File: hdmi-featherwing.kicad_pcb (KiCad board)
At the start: 2 copper layers, 22.9 x 50.8 mm, 10 parts, among them J1 HDMI_A

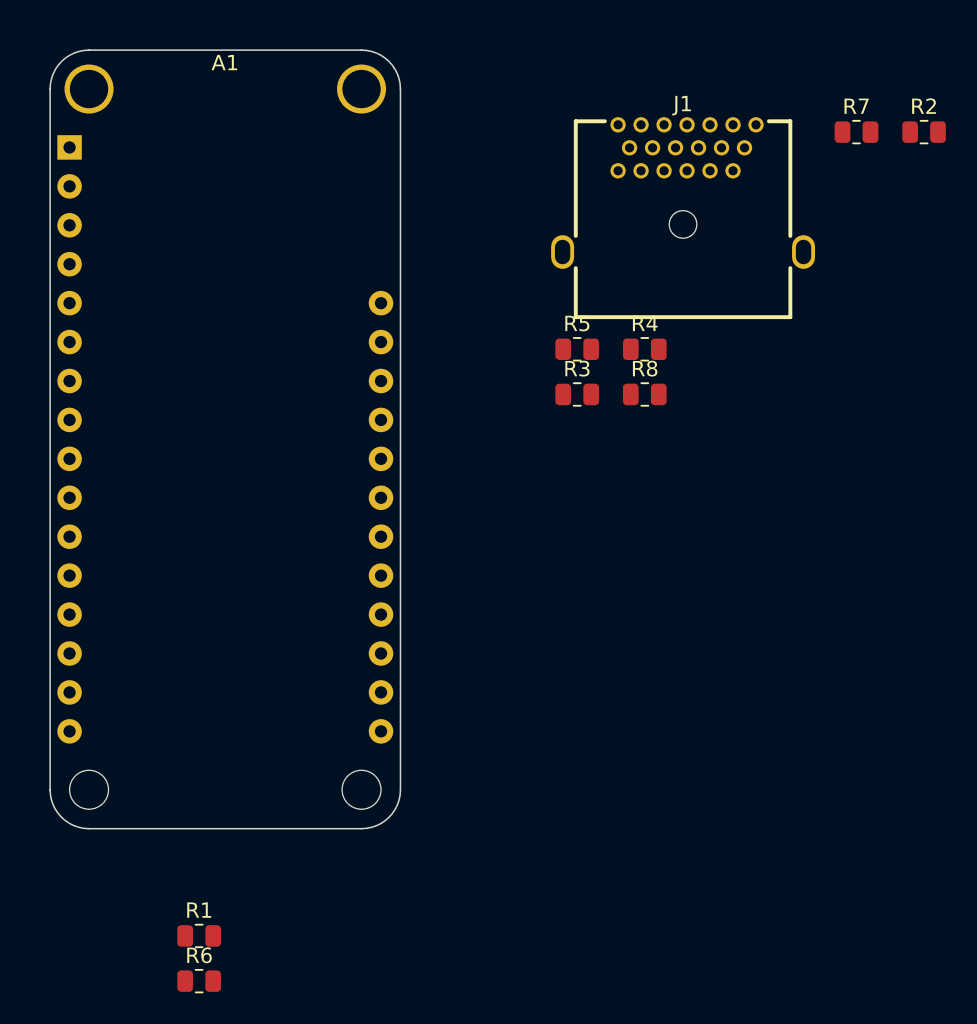
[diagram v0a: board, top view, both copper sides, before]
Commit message: Add CK resistors
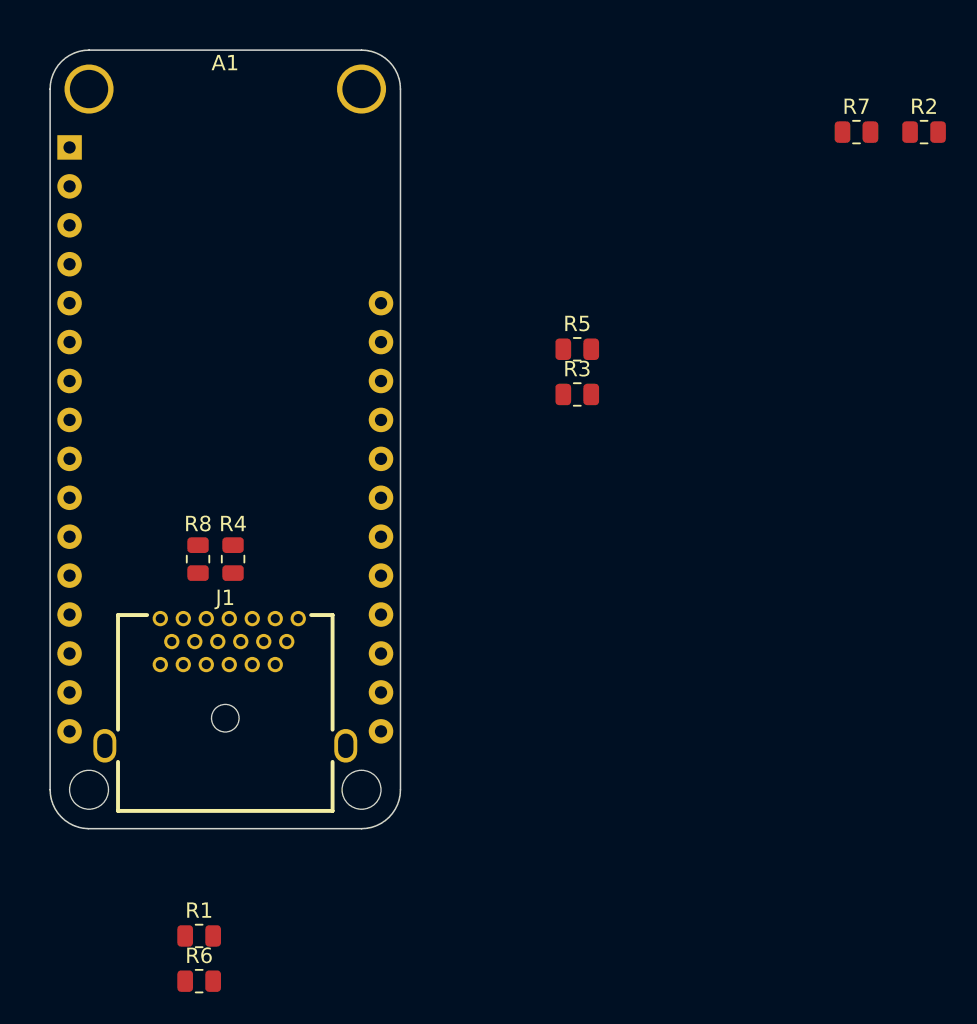
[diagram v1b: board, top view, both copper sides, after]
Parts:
- moved J1 43.9 mm to (119.4, 120.0)
- moved R8 31.1 mm to (117.6, 112.0), turned to -90 degrees
- moved R4 30.2 mm to (119.9, 112.0), turned to -90 degrees
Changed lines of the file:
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@@
   )
   (footprint "Resistor_SMD:R_0805_2012Metric" (layer "F.Cu")
-    (at 146.754 98.259)
-    (descr "Resistor SMD 0805 (2012 Metric), square (rectangular) end terminal, IPC_7351 nominal, (Body size source: IPC-SM-782 page 72, https://www.pcb-3d.com/wordpress/wp-content/uploads/ipc-sm-782a_amendment_1_and_2.pdf), generated with kicad-footprint-generator")
-    (tags "resistor")
-    (property "Sheetfile" "hdmi-featherwing.kicad_sch")
-    (property "Sheetname" "")
-    (attr smd)
-    (fp_text reference "R4" (at 0 -1.65) (layer "F.SilkS")
-      (effects (font (size 1 1) (thickness 0.15)))
-    )
-    (fp_text value "270" (at 0 1.65) (layer "F.Fab")
-      (effects (font (size 1 1) (thickness 0.15)))
-    )
-    (fp_text user "${REFERENCE}" (at 0 0) (layer "F.Fab")
-      (effects (font (size 0.5 0.5) (thickness 0.08)))
-    )
-    (fp_line (start -0.227064 -0.735) (end 0.227064 -0.735) (layer "F.SilkS") (width 0.12))
-    (fp_line (start -0.227064 0.735) (end 0.227064 0.735) (layer "F.SilkS") (width 0.12))
-    (fp_line (start 1.68 -0.95) (end 1.68 0.95) (layer "F.CrtYd") (width 0.05))
-    (fp_line (start 1.68 0.95) (end -1.68 0.95) (layer "F.CrtYd") (width 0.05))
-    (fp_line (start -1.68 -0.95) (end 1.68 -0.95) (layer "F.CrtYd") (width 0.05))
-    (fp_line (start -1.68 0.95) (end -1.68 -0.95) (layer "F.CrtYd") (width 0.05))
-    (fp_line (start 1 -0.625) (end 1 0.625) (layer "F.Fab") (width 0.1))
-    (fp_line (start 1 0.625) (end -1 0.625) (layer "F.Fab") (width 0.1))
-    (fp_line (start -1 0.625) (end -1 -0.625) (layer "F.Fab") (width 0.1))
-    (fp_line (start -1 -0.625) (end 1 -0.625) (layer "F.Fab") (width 0.1))
-    (pad "1" smd roundrect (at -0.9125 0) (locked) (size 1.025 1.4) (layers "F.Cu" "F.Paste" "F.Mask") (roundrect_rratio 0.243902)
+    (at 119.888 111.951 -90)
+    (descr "Resistor SMD 0805 (2012 Metric), square (rectangular) end terminal, IPC_7351 nominal, (Body size source: IPC-SM-782 page 72, https://www.pcb-3d.com/wordpress/wp-content/uploads/ipc-sm-782a_amendment_1_and_2.pdf), generated with kicad-footprint-generator")
+    (tags "resistor")
+    (property "Sheetfile" "hdmi-featherwing.kicad_sch")
+    (property "Sheetname" "")
+    (attr smd)
+    (fp_text reference "R4" (at -2.286 0 180) (layer "F.SilkS")
+      (effects (font (size 1 1) (thickness 0.15)))
+    )
+    (fp_text value "270" (at 0 1.650009 90) (layer "F.Fab") hide
+      (effects (font (size 1 1) (thickness 0.15)))
+    )
+    (fp_text user "${REFERENCE}" (at 0 0 90) (layer "F.Fab")
+      (effects (font (size 0.5 0.5) (thickness 0.08)))
+    )
+    (fp_line (start -0.227064 -0.735) (end 0.227064 -0.735) (layer "F.SilkS") (width 0.12))
+    (fp_line (start -0.227064 0.735) (end 0.227064 0.735) (layer "F.SilkS") (width 0.12))
+    (fp_line (start 1.68 -0.95) (end 1.68 0.95) (layer "F.CrtYd") (width 0.05))
+    (fp_line (start 1.68 0.95) (end -1.68 0.95) (layer "F.CrtYd") (width 0.05))
+    (fp_line (start -1.68 -0.95) (end 1.68 -0.95) (layer "F.CrtYd") (width 0.05))
+    (fp_line (start -1.68 0.95) (end -1.68 -0.95) (layer "F.CrtYd") (width 0.05))
+    (fp_line (start 1 -0.625) (end 1 0.625) (layer "F.Fab") (width 0.1))
+    (fp_line (start 1 0.625) (end -1 0.625) (layer "F.Fab") (width 0.1))
+    (fp_line (start -1 0.625) (end -1 -0.625) (layer "F.Fab") (width 0.1))
+    (fp_line (start -1 -0.625) (end 1 -0.625) (layer "F.Fab") (width 0.1))
+    (pad "1" smd roundrect (at -0.9125 0 270) (locked) (size 1.025 1.4) (layers "F.Cu" "F.Paste" "F.Mask") (roundrect_rratio 0.243902)
       (net 21 "/WING_CK+") (pintype "passive"))
-    (pad "2" smd roundrect (at 0.9125 0) (locked) (size 1.025 1.4) (layers "F.Cu" "F.Paste" "F.Mask") (roundrect_rratio 0.243902)
+    (pad "2" smd roundrect (at 0.9125 0 270) (locked) (size 1.025 1.4) (layers "F.Cu" "F.Paste" "F.Mask") (roundrect_rratio 0.243902)
       (net 35 "Net-(J1-Pad10)") (pintype "passive"))
     (model "${KICAD6_3DMODEL_DIR}/Resistor_SMD.3dshapes/R_0805_2012Metric.wrl"
@@
   )
   (footprint "HDMI:HDMI-TH_HYC12-HDMIA19-61" (layer "F.Cu")
-    (at 149.249 87.764)
+    (at 119.38 119.9815)
     (property "Sheetfile" "hdmi-featherwing.kicad_sch")
     (property "Sheetname" "")
@@
   )
   (footprint "Resistor_SMD:R_0805_2012Metric" (layer "F.Cu")
-    (at 146.754 101.209)
-    (descr "Resistor SMD 0805 (2012 Metric), square (rectangular) end terminal, IPC_7351 nominal, (Body size source: IPC-SM-782 page 72, https://www.pcb-3d.com/wordpress/wp-content/uploads/ipc-sm-782a_amendment_1_and_2.pdf), generated with kicad-footprint-generator")
-    (tags "resistor")
-    (property "Sheetfile" "hdmi-featherwing.kicad_sch")
-    (property "Sheetname" "")
-    (attr smd)
-    (fp_text reference "R8" (at 0 -1.65) (layer "F.SilkS")
-      (effects (font (size 1 1) (thickness 0.15)))
-    )
-    (fp_text value "270" (at 0 1.65) (layer "F.Fab")
-      (effects (font (size 1 1) (thickness 0.15)))
-    )
-    (fp_text user "${REFERENCE}" (at 0 0) (layer "F.Fab")
-      (effects (font (size 0.5 0.5) (thickness 0.08)))
-    )
-    (fp_line (start -0.227064 0.735) (end 0.227064 0.735) (layer "F.SilkS") (width 0.12))
-    (fp_line (start -0.227064 -0.735) (end 0.227064 -0.735) (layer "F.SilkS") (width 0.12))
-    (fp_line (start 1.68 0.95) (end -1.68 0.95) (layer "F.CrtYd") (width 0.05))
-    (fp_line (start -1.68 -0.95) (end 1.68 -0.95) (layer "F.CrtYd") (width 0.05))
-    (fp_line (start 1.68 -0.95) (end 1.68 0.95) (layer "F.CrtYd") (width 0.05))
-    (fp_line (start -1.68 0.95) (end -1.68 -0.95) (layer "F.CrtYd") (width 0.05))
-    (fp_line (start 1 -0.625) (end 1 0.625) (layer "F.Fab") (width 0.1))
-    (fp_line (start -1 -0.625) (end 1 -0.625) (layer "F.Fab") (width 0.1))
-    (fp_line (start 1 0.625) (end -1 0.625) (layer "F.Fab") (width 0.1))
-    (fp_line (start -1 0.625) (end -1 -0.625) (layer "F.Fab") (width 0.1))
-    (pad "1" smd roundrect (at -0.9125 0) (locked) (size 1.025 1.4) (layers "F.Cu" "F.Paste" "F.Mask") (roundrect_rratio 0.243902)
+    (at 117.602 111.951 -90)
+    (descr "Resistor SMD 0805 (2012 Metric), square (rectangular) end terminal, IPC_7351 nominal, (Body size source: IPC-SM-782 page 72, https://www.pcb-3d.com/wordpress/wp-content/uploads/ipc-sm-782a_amendment_1_and_2.pdf), generated with kicad-footprint-generator")
+    (tags "resistor")
+    (property "Sheetfile" "hdmi-featherwing.kicad_sch")
+    (property "Sheetname" "")
+    (attr smd)
+    (fp_text reference "R8" (at -2.286 0 180) (layer "F.SilkS")
+      (effects (font (size 1 1) (thickness 0.15)))
+    )
+    (fp_text value "270" (at 0.000005 1.650009 90) (layer "F.Fab") hide
+      (effects (font (size 1 1) (thickness 0.15)))
+    )
+    (fp_text user "${REFERENCE}" (at 0 0 90) (layer "F.Fab")
+      (effects (font (size 0.5 0.5) (thickness 0.08)))
+    )
+    (fp_line (start -0.227064 0.735) (end 0.227064 0.735) (layer "F.SilkS") (width 0.12))
+    (fp_line (start -0.227064 -0.735) (end 0.227064 -0.735) (layer "F.SilkS") (width 0.12))
+    (fp_line (start 1.68 0.95) (end -1.68 0.95) (layer "F.CrtYd") (width 0.05))
+    (fp_line (start -1.68 -0.95) (end 1.68 -0.95) (layer "F.CrtYd") (width 0.05))
+    (fp_line (start 1.68 -0.95) (end 1.68 0.95) (layer "F.CrtYd") (width 0.05))
+    (fp_line (start -1.68 0.95) (end -1.68 -0.95) (layer "F.CrtYd") (width 0.05))
+    (fp_line (start 1 -0.625) (end 1 0.625) (layer "F.Fab") (width 0.1))
+    (fp_line (start -1 -0.625) (end 1 -0.625) (layer "F.Fab") (width 0.1))
+    (fp_line (start 1 0.625) (end -1 0.625) (layer "F.Fab") (width 0.1))
+    (fp_line (start -1 0.625) (end -1 -0.625) (layer "F.Fab") (width 0.1))
+    (pad "1" smd roundrect (at -0.9125 0 270) (locked) (size 1.025 1.4) (layers "F.Cu" "F.Paste" "F.Mask") (roundrect_rratio 0.243902)
       (net 22 "/WING_CK-") (pintype "passive"))
-    (pad "2" smd roundrect (at 0.9125 0) (locked) (size 1.025 1.4) (layers "F.Cu" "F.Paste" "F.Mask") (roundrect_rratio 0.243902)
+    (pad "2" smd roundrect (at 0.9125 0 270) (locked) (size 1.025 1.4) (layers "F.Cu" "F.Paste" "F.Mask") (roundrect_rratio 0.243902)
       (net 34 "Net-(J1-Pad12)") (pintype "passive"))
     (model "${KICAD6_3DMODEL_DIR}/Resistor_SMD.3dshapes/R_0805_2012Metric.wrl"

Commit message: Label differential pair nets
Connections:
- net Net-(J1-Pad1) renamed /D2+
- net Net-(J1-Pad10) renamed /CK+
- net Net-(J1-Pad12) renamed /CK-
- net Net-(J1-Pad3) renamed /D2-
- net Net-(J1-Pad4) renamed /D1+
- net Net-(J1-Pad6) renamed /D1-
- net Net-(J1-Pad7) renamed /D0+
- net Net-(J1-Pad9) renamed /D0-

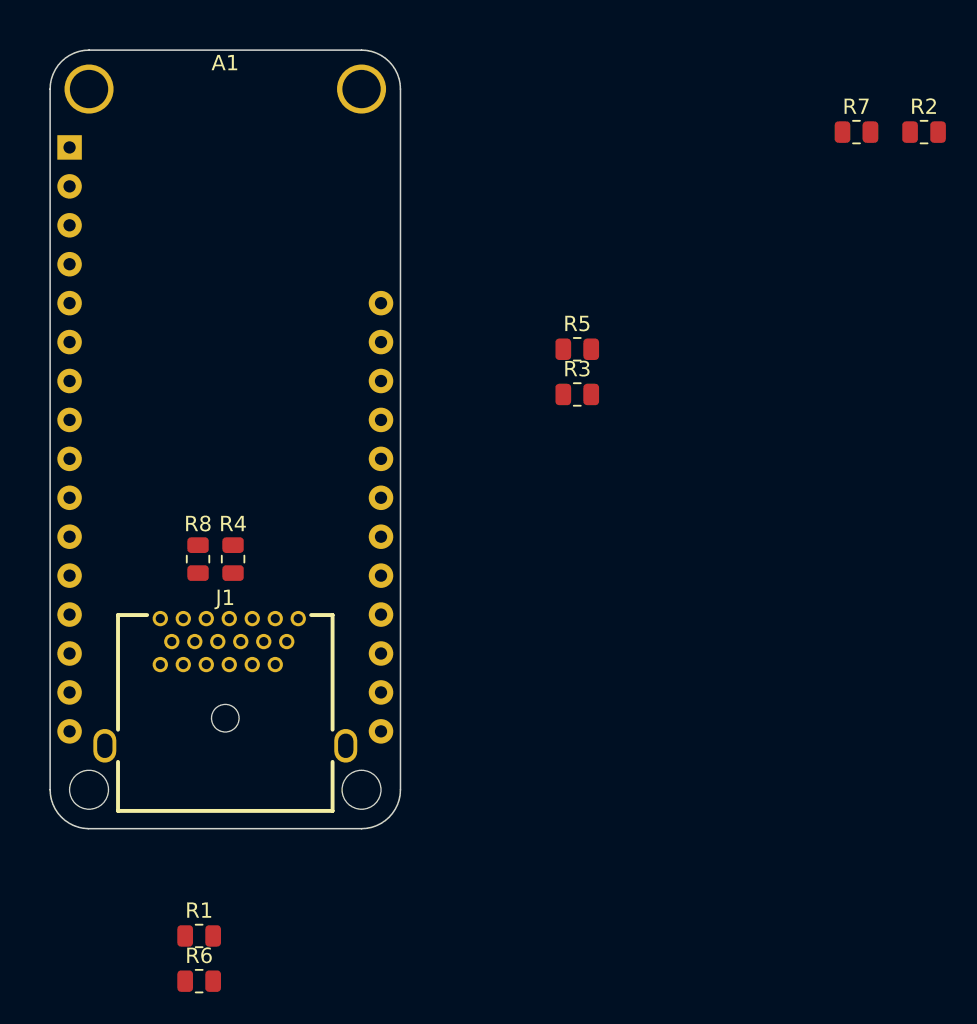
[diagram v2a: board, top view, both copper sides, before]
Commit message: Route resistors
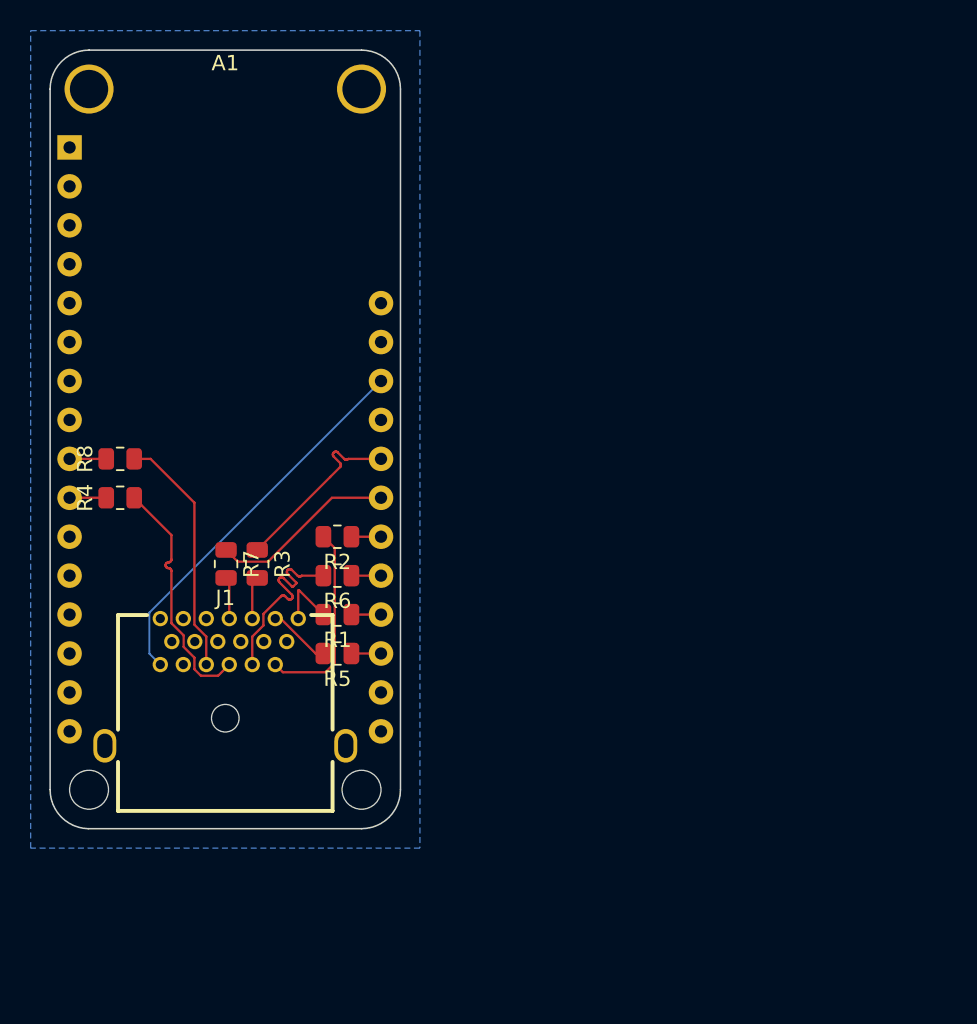
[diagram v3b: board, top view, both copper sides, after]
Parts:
- moved R7 49.9 mm to (119.4, 112.3), turned to -90 degrees
- moved R2 46.5 mm to (126.7, 110.5), turned to 180 degrees
- moved R6 28.0 mm to (126.7, 113.0), turned to 180 degrees
- moved R5 25.3 mm to (126.7, 118.1), turned to 180 degrees
- moved R3 23.6 mm to (121.5, 112.3), turned to -90 degrees
- moved R1 22.8 mm to (126.7, 115.6), turned to 180 degrees
- moved R4 8.38 mm to (112.5, 108.0), turned to 0 degrees
- moved R8 8.28 mm to (112.5, 105.4), turned to 0 degrees
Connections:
- A1 pad 10: /WING_CK- -> /WING_CK+
- A1 pad 19: /WING_D2+ -> /WING_D2-
- A1 pad 20: /WING_D2- -> /WING_D2+
- A1 pad 21: /WING_D1+ -> /WING_D1-
- A1 pad 22: /WING_D1- -> /WING_D1+
- A1 pad 23: /WING_D0+ -> /WING_D0-
- A1 pad 24: /WING_D0- -> /WING_D0+
- A1 pad 9: /WING_CK+ -> /WING_CK-
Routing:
- net +5V: track 0.00 -> 25.1 mm
- net /CK+: track 0.00 -> 16.0 mm
- net /CK-: track 0.00 -> 16.0 mm
- net /D1-: track 0.00 -> 12.9 mm
- net /D1+: track 0.00 -> 12.9 mm
- net /WING_D0+: track 0.00 -> 12.1 mm
- net /WING_D0-: track 0.00 -> 12.1 mm
- net /D2+: track 0.00 -> 4.13 mm
- net /D2-: track 0.00 -> 4.09 mm
- net /D0+: track 0.00 -> 2.78 mm
- net /D0-: track 0.00 -> 2.74 mm
- net /WING_CK-: track 0.00 -> 2.39 mm
- net /WING_CK+: track 0.00 -> 2.39 mm
- net /WING_D1+: track 0.00 -> 1.93 mm
- net /WING_D2-: track 0.00 -> 1.93 mm
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- added copper zone on B.Cu, net GND

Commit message: Fix violations
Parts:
- moved R5 1.39 mm to (127.6, 119.2), turned to -90 degrees
- moved R1 0.93 mm to (127.6, 115.7), turned to 90 degrees
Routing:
- net /D2-: track 4.09 -> 6.72 mm
- net /D2+: track 4.13 -> 6.72 mm
- net /WING_D2+: track 1.93 -> 3.31 mm
- net /WING_D2-: track 1.93 -> 3.31 mm

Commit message: Silkscreen
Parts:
- added Ferris: G*****, Rustacean:Ferris, F.Cu at (119.4, 94.0)
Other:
- board text added: "*probably not DVI either"
- board text added: "Not HDMI* Featherwing"
- board text added: "r1"
